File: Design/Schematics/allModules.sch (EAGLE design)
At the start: 178 parts, among them IC1 MAX7219CNG, IC2 MAX7219CNG, IC3 MAX7219CNG, IC4 MAX7219CNG, SW1 arcade_btn, SW2 arcade_btn, SW3 arcade_btn, SW4 arcade_btn, U1 328P, U2 328P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

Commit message: Update schematic
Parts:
- removed CLOCK_MINS, DIS1: HD-K121, display-hp:HD-K121
- removed CN6: (no value), con-hdrs40:HDR-1X5-SIP-100
- removed S1: (no value), switch:320-938
- added CN8: (no value), con-hdrs40:HDR-1X5-SIP-100
- added DIGIT_1, DIGIT_2, DIGIT_3, DIGIT_4: HD-H103, display-hp:HD-H103
- added S2: (no value), switch:320-938
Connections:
- removed net N$141: CN6.4, S1B.S
- removed net N$142: CN6.2, S11.S
- removed net N$15: CLOCK_MINS.CA2, IC1.DIG1
- removed net N$16: CLOCK_MINS.CA1, IC1.DIG0
- removed net N$32: S11.O, U$2.TX
- removed net N$33: S1B.O, U$2.RX
- new net ESP_RX: S2B.O, U$2.RX
- new net ESP_TX: S21.O, U$2.TX
- new net N$143: CN8.2, S21.S
- new net N$17: CN8.4, S2B.S
- new net N$18: DIGIT_3.CC, DIGIT_3.CC@1, IC1.DIG2
- new net N$19: DIGIT_4.CC, DIGIT_4.CC@1, IC1.DIG3
- net GND: now also CN8.1; no longer CN6.1
- net MAI_RST: now also CN8.3; no longer CN6.3
- net MEGA_RX: now also S21.P; no longer S11.P
- net MEGA_TX: now also S2B.P; no longer S1B.P
- net N$1: now also DIGIT_1.A, DIGIT_2.A, DIGIT_3.A, DIGIT_4.A; no longer CLOCK_MINS.A1, CLOCK_MINS.A2, DIS1.A1, DIS1.A2
- net N$13: now also DIGIT_2.CC, DIGIT_2.CC@1, IC1.DIG1; no longer DIS1.CA2, IC1.DIG3
- net N$14: now also DIGIT_1.CC, DIGIT_1.CC@1, IC1.DIG0; no longer DIS1.CA1, IC1.DIG2
- net N$2: now also DIGIT_1.B, DIGIT_2.B, DIGIT_3.B, DIGIT_4.B; no longer CLOCK_MINS.B1, CLOCK_MINS.B2, DIS1.B1, DIS1.B2
- net N$3: now also DIGIT_1.C, DIGIT_2.C, DIGIT_3.C, DIGIT_4.C; no longer CLOCK_MINS.C1, CLOCK_MINS.C2, DIS1.C1, DIS1.C2
- net N$4: now also DIGIT_1.D, DIGIT_2.D, DIGIT_3.D, DIGIT_4.D; no longer CLOCK_MINS.D1, CLOCK_MINS.D2, DIS1.D1, DIS1.D2
- net N$5: now also DIGIT_1.E, DIGIT_2.E, DIGIT_3.E, DIGIT_4.E; no longer CLOCK_MINS.E1, CLOCK_MINS.E2, DIS1.E1, DIS1.E2
- net N$6: now also DIGIT_1.F, DIGIT_2.F, DIGIT_3.F, DIGIT_4.F; no longer CLOCK_MINS.F1, CLOCK_MINS.F2, DIS1.F1, DIS1.F2
- net N$7: now also DIGIT_1.G, DIGIT_2.G, DIGIT_3.G, DIGIT_4.G; no longer CLOCK_MINS.G1, CLOCK_MINS.G2, DIS1.G1, DIS1.G2
- net VCC: now also CN8.5; no longer CN6.5
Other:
- moved on the sheet: CN7

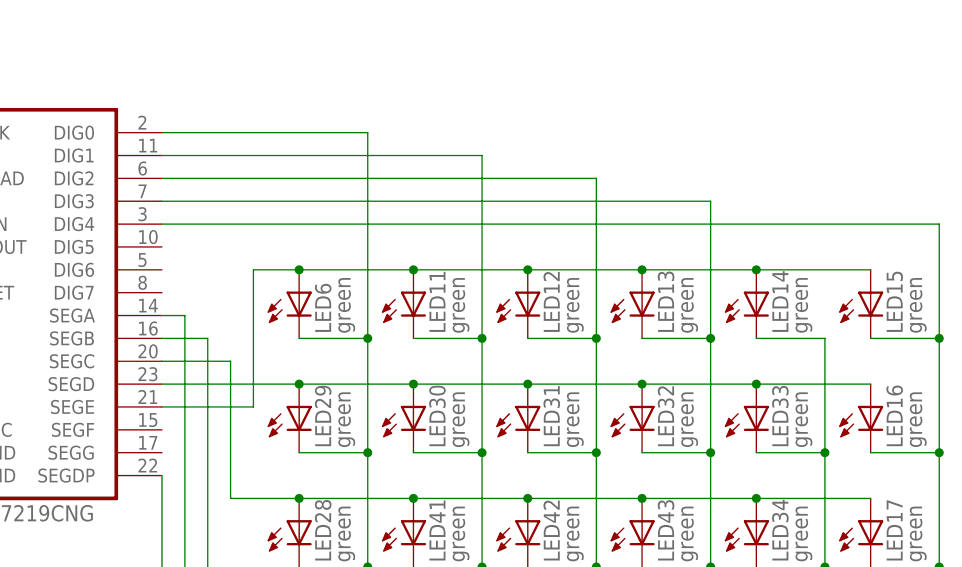
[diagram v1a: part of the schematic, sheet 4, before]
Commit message: Added missing wire to maze module
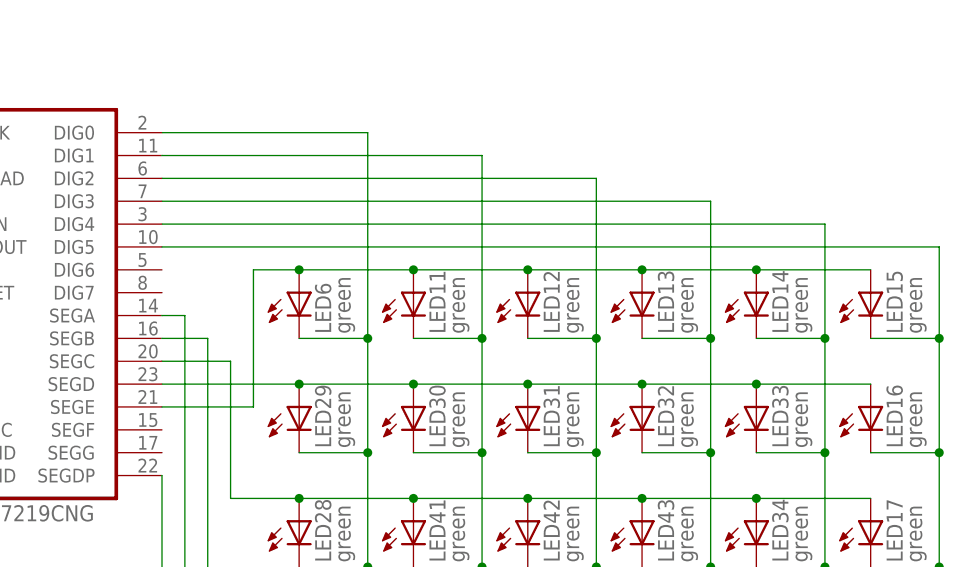
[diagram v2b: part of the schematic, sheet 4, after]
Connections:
- net N$57: now also IC2.DIG4
- net N$58: now also IC2.DIG5; no longer IC2.DIG4
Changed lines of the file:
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@@
 <pinref part="LED35" gate="G$1" pin="C"/>
 <pinref part="LED36" gate="G$1" pin="C"/>
+<pinref part="IC2" gate="G$1" pin="DIG4"/>
+<wire x1="25.4" y1="15.24" x2="99.06" y2="15.24" width="0.1524" layer="91"/>
+<wire x1="99.06" y1="15.24" x2="99.06" y2="2.54" width="0.1524" layer="91"/>
+<junction x="99.06" y="2.54"/>
 </segment>
 </net>
@@
 <junction x="111.76" y="-10.16"/>
 <wire x1="104.14" y1="2.54" x2="111.76" y2="2.54" width="0.1524" layer="91"/>
-<pinref part="IC2" gate="G$1" pin="DIG4"/>
-<wire x1="25.4" y1="15.24" x2="111.76" y2="15.24" width="0.1524" layer="91"/>
-<wire x1="111.76" y1="15.24" x2="111.76" y2="2.54" width="0.1524" layer="91"/>
 <junction x="111.76" y="2.54"/>
 <pinref part="LED15" gate="G$1" pin="C"/>
@@
 <pinref part="LED19" gate="G$1" pin="C"/>
 <pinref part="LED20" gate="G$1" pin="C"/>
+<pinref part="IC2" gate="G$1" pin="DIG5"/>
+<wire x1="111.76" y1="12.7" x2="111.76" y2="2.54" width="0.1524" layer="91"/>
+<wire x1="25.4" y1="12.7" x2="111.76" y2="12.7" width="0.1524" layer="91"/>
 </segment>
 </net>

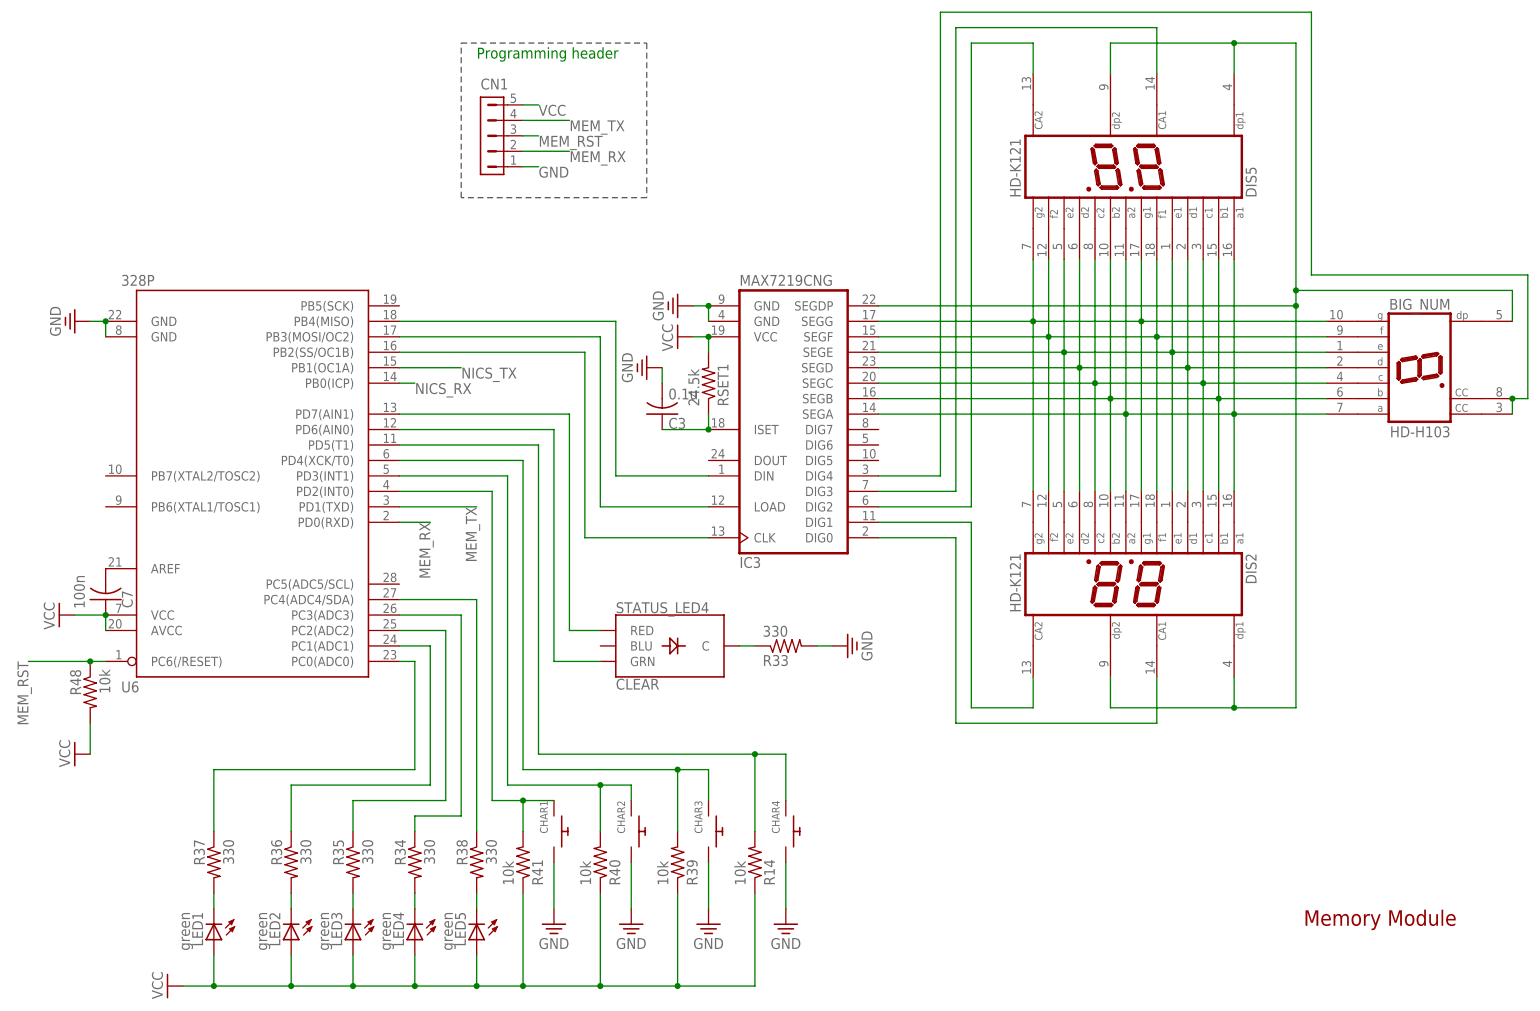
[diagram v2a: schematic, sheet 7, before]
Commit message: Change schematic to accurately reflect how clear leds work
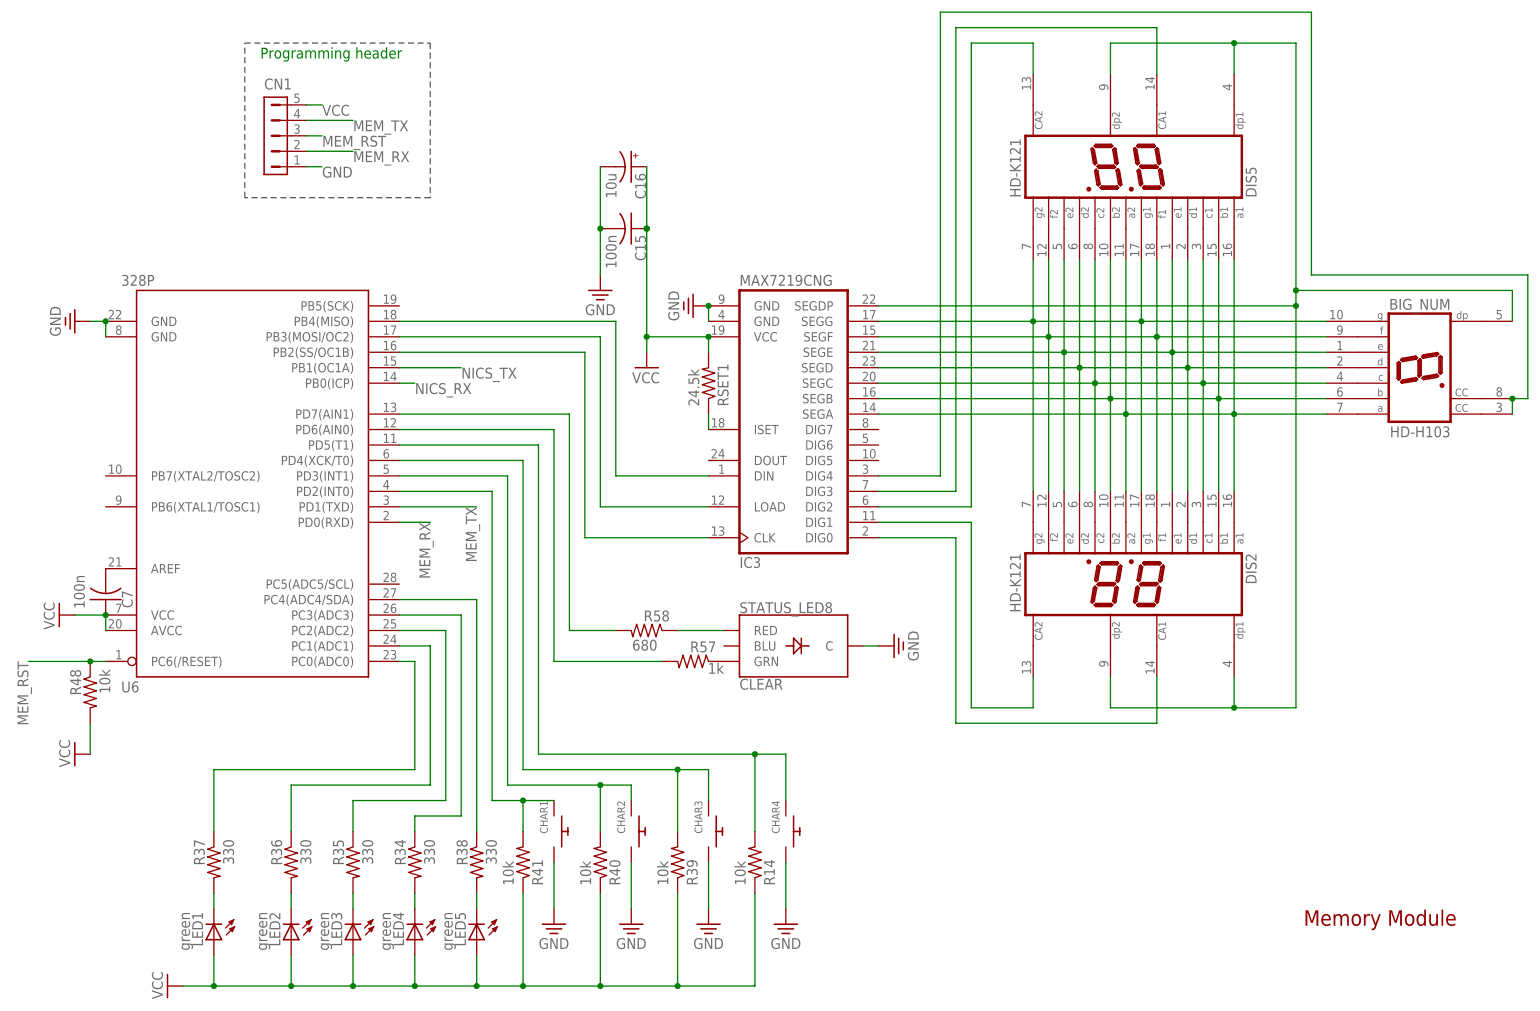
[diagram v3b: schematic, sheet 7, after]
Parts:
- removed C3: 0.1u, adafruit:C-US025-024X044
- removed R20, R21, R29, R33: 330, adafruit:R-US_0309/12
- removed STATUS_LED, STATUS_LED1, STATUS_LED3, STATUS_LED4: CLEAR, SparkFun-LED:LED-RGB-CCCLEAR
- added C15: 100n, adafruit:C-US025-024X044
- added C16: 10u, adafruit:CPOL-US085CS-1AR
- added R49: 100, adafruit:R-US_0309/12
- added R50, R52, R54, R56, R58: 680, adafruit:FLIPFLOP-RES
- added R51, R53, R55, R57: 1k, adafruit:FLIPFLOP-RES
- added STATUS_LED5, STATUS_LED6, STATUS_LED7, STATUS_LED8: CLEAR, SparkFun-LED:LED-RGB-CCCLEAR
- R28: value 330 -> 1k; device adafruit:R-US_0309/12 -> adafruit:FLIPFLOP-RES
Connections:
- removed net N$69: R20.1, STATUS_LED.C
- removed net N$72: R21.1, STATUS_LED1.C
- removed net N$77: R29.1, STATUS_LED3.C
- removed net N$78: STATUS_LED3.GRN, U5.PD2(INT0)
- removed net N$90: R33.1, STATUS_LED4.C
- new net N$144: R51.1, STATUS_LED5.GRN
- new net N$145: R52.1, STATUS_LED5.RED
- new net N$149: R53.1, STATUS_LED6.GRN
- new net N$15: BUZZER.-, R49.1
- new net N$150: R54.1, STATUS_LED6.RED
- new net N$152: R55.2, U5.PD2(INT0)
- new net N$154: R55.1, STATUS_LED7.GRN
- new net N$155: R56.1, STATUS_LED7.RED
- new net N$159: R57.1, STATUS_LED8.GRN
- new net N$16: R28.1, STATUS_LED2.GRN
- new net N$160: R58.1, STATUS_LED8.RED
- new net N$32: R50.1, STATUS_LED2.RED
- net GND: now also C15.2, C16.-, R49.2, STATUS_LED5.C, STATUS_LED6.C, STATUS_LED7.C, STATUS_LED8.C; no longer BUZZER.-, C3.2, R20.2, R21.2, R28.2, R29.2, R33.2
- net N$100: now also R58.2; no longer STATUS_LED4.RED
- net N$110: no longer C3.1
- net N$21: no longer R28.1
- net N$67: now also R54.2; no longer STATUS_LED.RED
- net N$68: now also R53.2; no longer STATUS_LED.GRN
- net N$70: now also R52.2; no longer STATUS_LED1.RED
- net N$71: now also R51.2; no longer STATUS_LED1.GRN
- net N$75: now also R28.2; no longer STATUS_LED2.GRN
- net N$76: now also R50.2; no longer STATUS_LED2.RED
- net N$79: now also R56.2; no longer STATUS_LED3.BLU
- net N$99: now also R57.2; no longer STATUS_LED4.GRN
- net VCC: now also C15.1, C16.+
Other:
- moved on the sheet: CN1, R28, STATUS_LED2

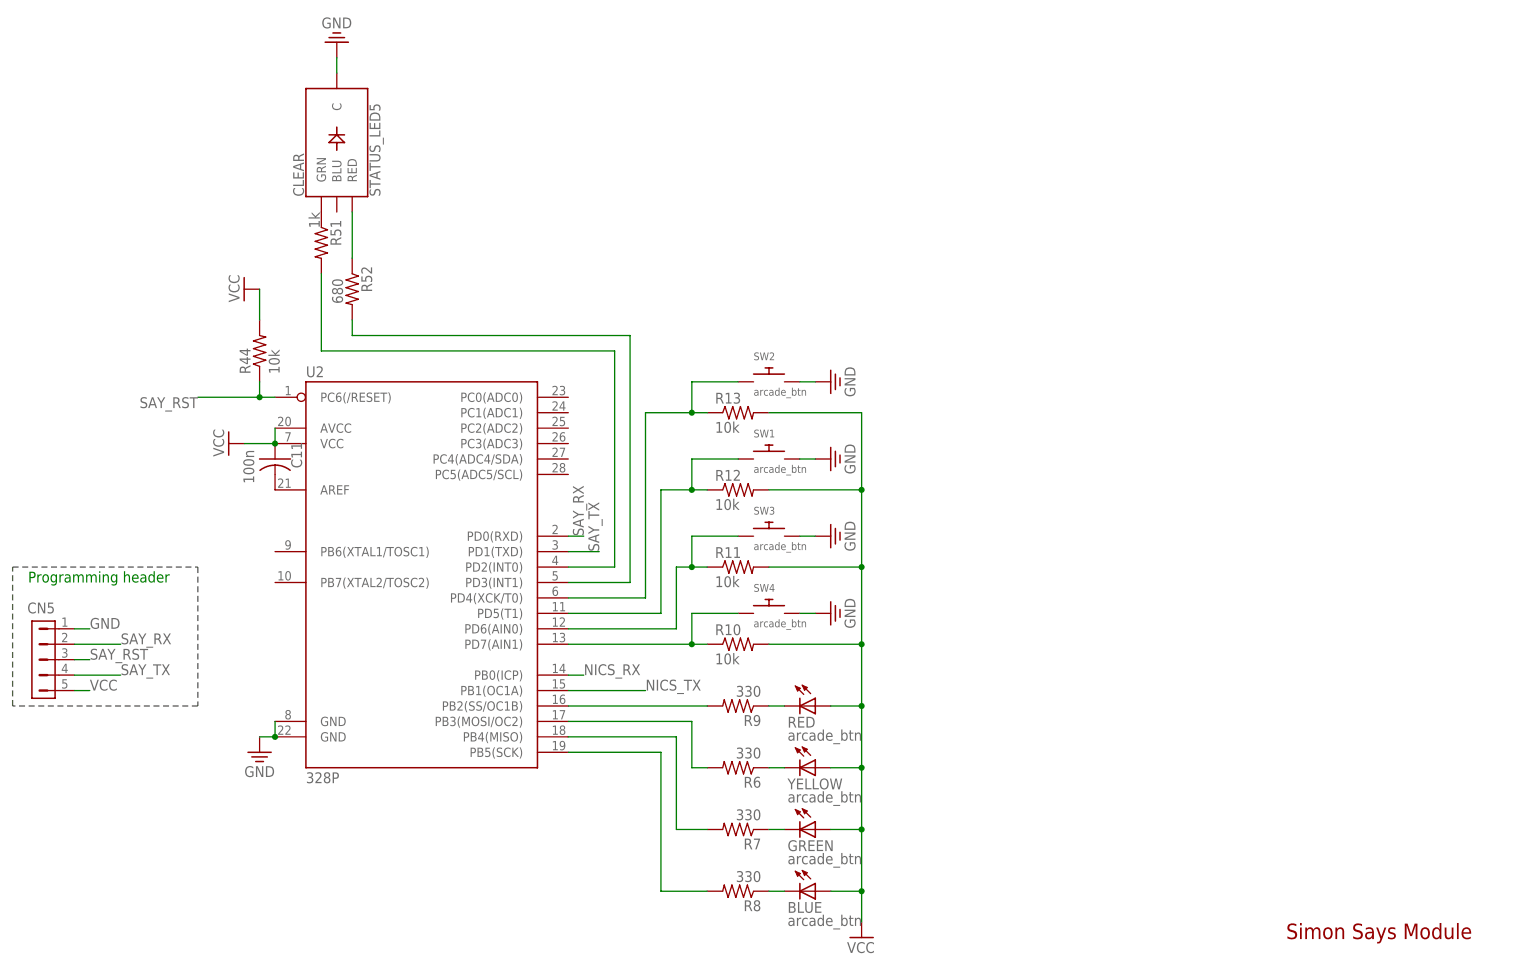
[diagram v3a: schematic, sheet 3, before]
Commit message: Added buzzer to simon says module
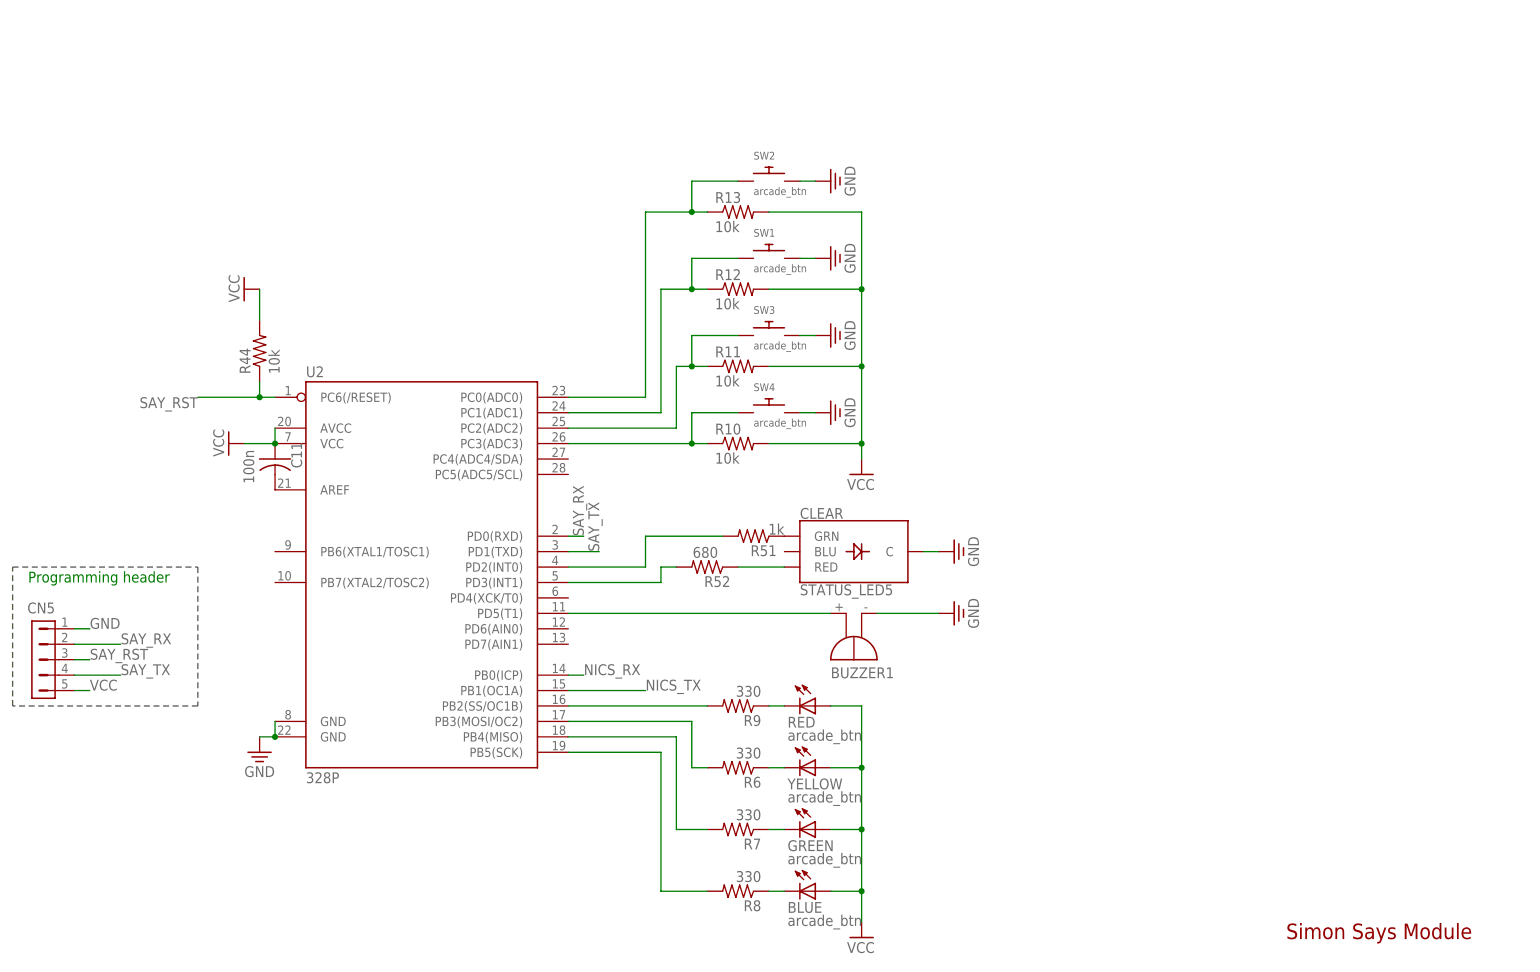
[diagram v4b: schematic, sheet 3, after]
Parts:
- added BUZZER1: EB2209A, buzzer:EB2209A
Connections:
- new net N$33: BUZZER1.+, U2.PD5(T1)
- net GND: now also BUZZER1.-
- net N$34: now also U2.PC3(ADC3); no longer U2.PD7(AIN1)
- net N$35: now also U2.PC2(ADC2); no longer U2.PD6(AIN0)
- net N$38: now also U2.PC1(ADC1); no longer U2.PD5(T1)
- net N$39: now also U2.PC0(ADC0); no longer U2.PD4(XCK/T0)
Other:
- moved on the sheet: R10, R11, R12, R13, R51, R52, STATUS_LED5, SW1, SW2, SW3, SW4
